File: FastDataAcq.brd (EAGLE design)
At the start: 114.3 x 62.7 mm, 224 parts, among them IC1 LT1963AEQ, IC2 FT230XQ, IC3 ADCMP553BRMZ, J1 MICRO-FIT_3.0_2POS_RA_SMD, J2 USB_MICROAB_SMT, J3 HEADER_0.1"_10P_2R_SMT, X1 87832-14, X2 SMA-142-0701-801/806, X3 SMA-142-0701-801/806, Y1 SI530-500, Y2 100MHz, Y3 DNP

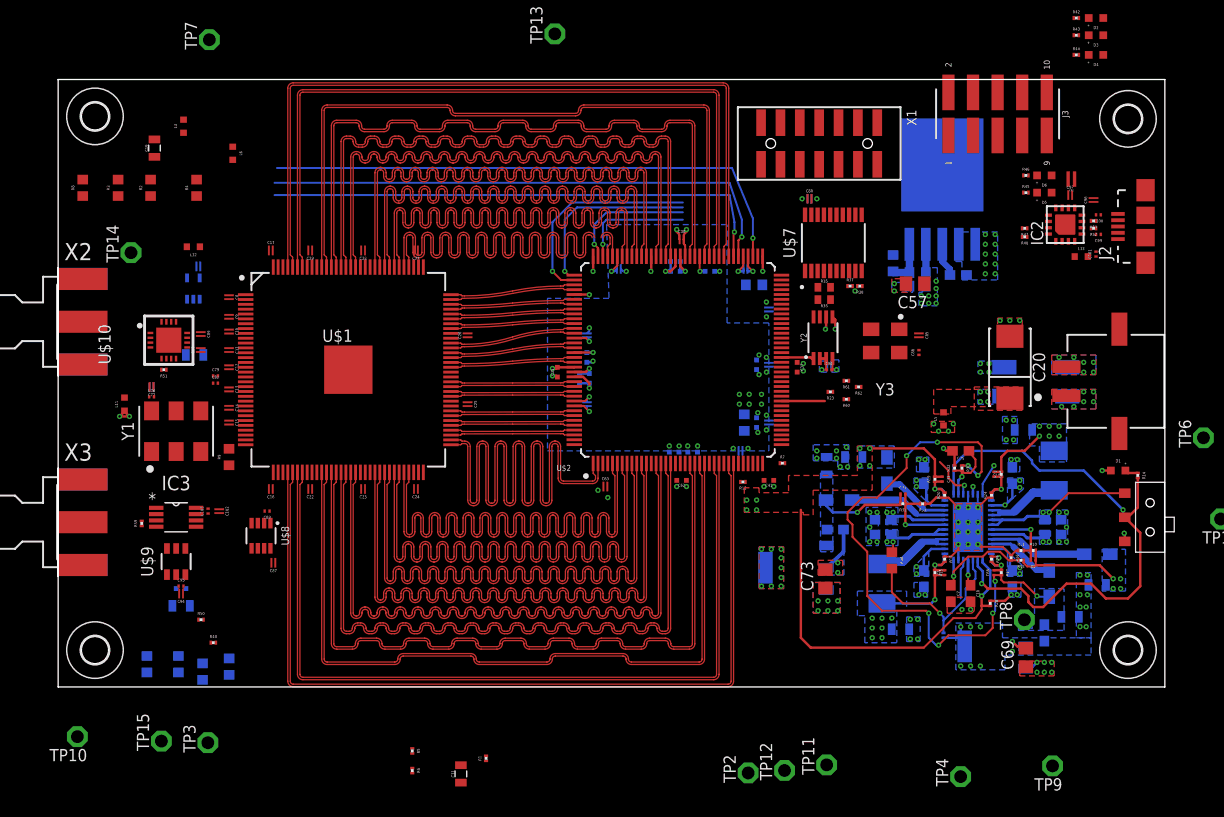
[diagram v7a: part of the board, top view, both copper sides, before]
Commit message: Digital routing almost done.
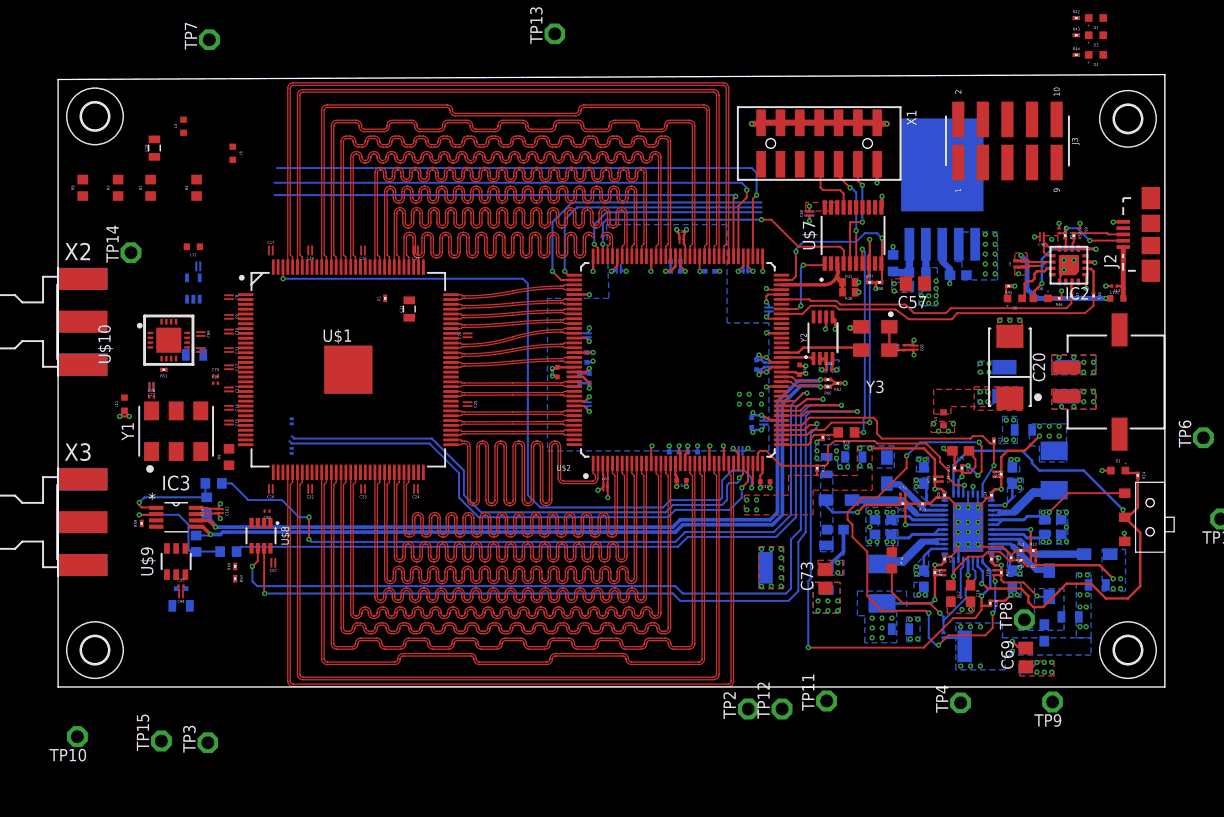
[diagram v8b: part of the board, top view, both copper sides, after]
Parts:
- removed R34: NA, rcl:R0603
- moved R1 48.6 mm to (33.8, 57.4)
- moved C31 48.3 mm to (36.3, 56.3)
- moved R6 38.2 mm to (24.1, 44.7), flipped to the bottom
- moved R5 33.4 mm to (24.1, 41.7), flipped to the bottom
- moved R54 19.5 mm to (16.1, 38.3), turned to 0 degrees
- moved R23 17.6 mm to (96.6, 42.7), turned to 270 degrees
- moved R57 16.8 mm to (15.4, 36.0), turned to 270 degrees
- moved R56 13.4 mm to (14.3, 32.1)
- moved R46 13.2 mm to (103.4, 57.4), turned to 180 degrees
- moved R55 12.7 mm to (17.6, 31.3), turned to 0 degrees
- moved D6 12.7 mm to (101.5, 57.4), turned to 0 degrees
- moved D5 11.3 mm to (98.8, 57.4)
- moved R39 10.6 mm to (81.4, 43.6), flipped to the top, turned to 180 degrees
- moved C92 10.2 mm to (99.4, 61.0), turned to 270 degrees
- moved R45 9.81 mm to (98.2, 58.7), turned to 180 degrees
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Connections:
- new net N3: U$2.P$62
- new net N4: U$2.P$61
- new net N5: U$2.P$59
- new net N6: U$2.P$58
- new net N7: U$2.P$57
- new net N8: U$2.P$48
- new net N9: U$2.P$47
- net 3V3: no longer R34.2
- net ADC_PWR_EN: now also U$2.P$41; no longer U$2.P$48
- net ANALOG_PWR_EN: now also U$2.P$40; no longer U$2.P$47
- net FPGA_CCLK: no longer R34.1
- net FPGA_GPIO1: no longer U$2.P$57
- net FPGA_GPIO2: no longer U$2.P$58
- net FPGA_GPIO3: no longer U$2.P$59
- net FPGA_GPIO4: no longer U$2.P$61
- net FPGA_GPIO5: no longer U$2.P$62
- net FPGA_GPIO6: no longer U$2.P$64
- net FPGA_GPIO7: no longer U$2.P$67
- net FPGA_RXD: now also U$2.P$67; no longer U$2.P$41
- net FPGA_TXD: now also U$2.P$64; no longer U$2.P$40
- net GND: now also IC2.TAB
- net TRIG_RESET_HIGH: now also U$2.P$45; no longer U$2.P$46
- net TRIG_RESET_LOW: now also U$2.P$46; no longer U$2.P$45
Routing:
- net FPGA_SCL: track 0.00 -> 92.4 mm, vias 0 -> 2
- net FPGA_SDA: track 0.00 -> 89.4 mm, vias 0 -> 2
- net FPGA_TRIG+: track 0.00 -> 84.3 mm, vias 0 -> 2
- net FPGA_TRIG-: track 0.00 -> 84.2 mm, vias 0 -> 2
- net TRIG_RESET_LOW: track 0.00 -> 80.2 mm, vias 0 -> 3
- net ADC_CALRUN: track 0.00 -> 78.7 mm, vias 0 -> 2
- net TRIG_RESET_HIGH: track 4.47 -> 78.1 mm, vias 0 -> 1
- net GND: track 64.3 -> 122.2 mm, vias 116 -> 140
- net ADC_PD: track 0.00 -> 56.1 mm, vias 0 -> 1
- net ADC_CAL: track 0.00 -> 55.1 mm, vias 0 -> 1
- net FPGA_TXD: track 0.00 -> 34.4 mm
- net FPGA_INITB: track 0.00 -> 33.1 mm, vias 0 -> 2
- net 3V3: track 19.3 -> 51.8 mm, vias 21 -> 27
- net FPGA_RXD: track 0.00 -> 31.5 mm
- net ADC_PWR_EN: track 3.28 -> 29.9 mm
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- added copper zone on layer 1, net 3V3
- added copper zone on layer 1, net 3V3OUT
- added copper zone on layer 3, net 3V3OUT
- added copper zone on layer 1, net 5VUSB
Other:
- board size 114.3 x 62.7 mm -> 114.3 x 63.2 mm
